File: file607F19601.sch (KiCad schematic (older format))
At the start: 14 parts, among them SW2 SW_SPDT, U2 MP2235

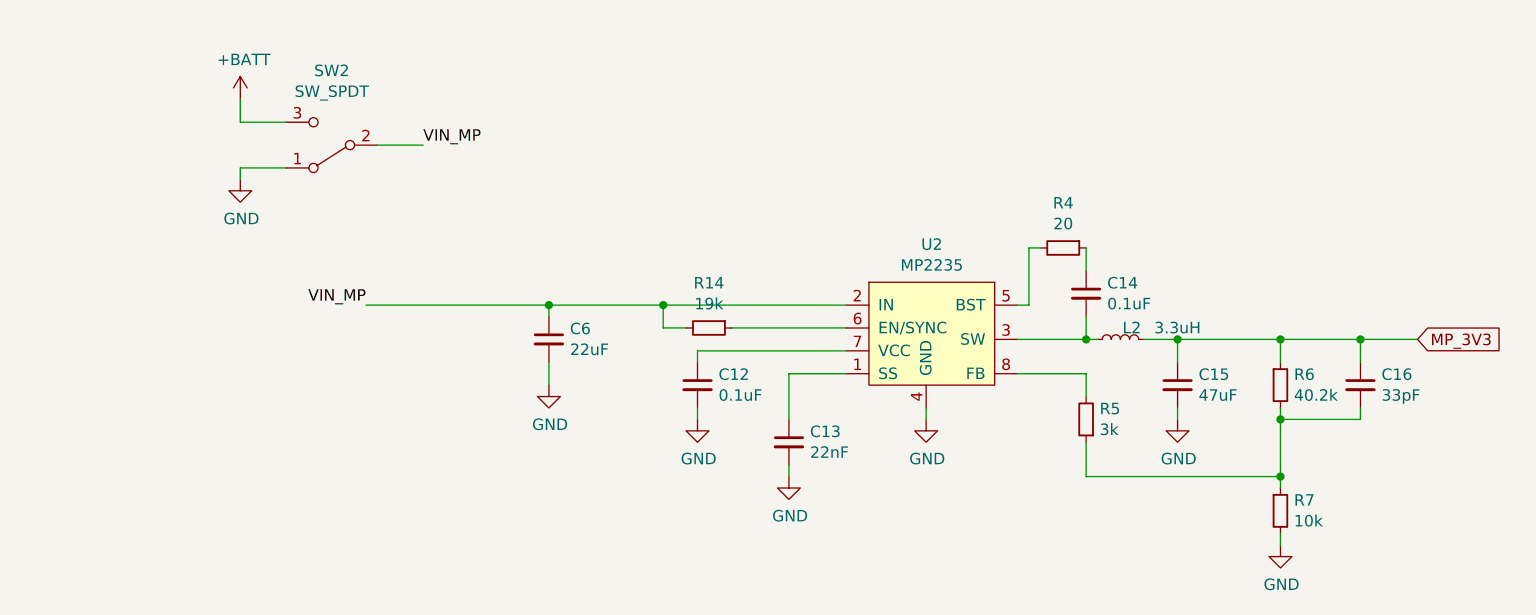
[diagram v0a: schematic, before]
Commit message: added data logging
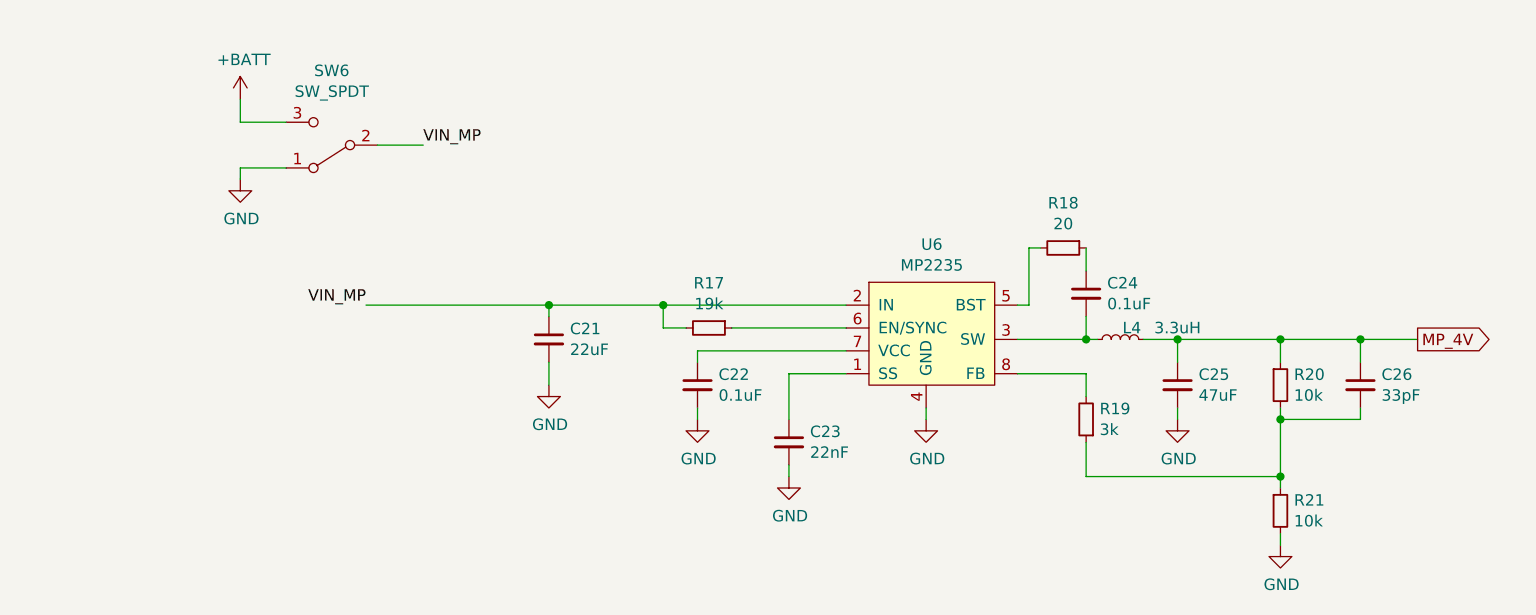
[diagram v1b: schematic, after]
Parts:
- R6: value 40.2k -> 10k
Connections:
- net MP_3V3 renamed MP_4V
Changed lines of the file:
@@
 $Descr A4 11693 8268
 encoding utf-8
-Sheet 4 10
+Sheet 9 10
 Title ""
 Date ""
@@
 AR Path="/607D64D2/607F1961/607F2E5A" Ref="C6"  Part="1"
 AR Path="/608CA2DC/608CBCF1/607F2E5A" Ref="C21"  Part="1"
-F 0 "C6" H 3342 3246 50  0000 L CNN
+F 0 "C21" H 3342 3246 50  0000 L CNN
 F 1 "22uF" H 3342 3155 50  0000 L CNN
 F 2 "" H 3250 3200 50  0001 C CNN
@@
 AR Path="/607D64D2/607F1961/607F34C1" Ref="#PWR05"  Part="1"
 AR Path="/608CA2DC/608CBCF1/607F34C1" Ref="#PWR0103"  Part="1"
-F 0 "#PWR05" H 3250 3150 50  0001 C CNN
+F 0 "#PWR0103" H 3250 3150 50  0001 C CNN
 F 1 "GND" H 3255 3227 50  0000 C CNN
 F 2 "" H 3250 3400 50  0001 C CNN
@@
 AR Path="/607D64D2/607F1961/60826F0B" Ref="C12"  Part="1"
 AR Path="/608CA2DC/608CBCF1/60826F0B" Ref="C22"  Part="1"
-F 0 "C12" H 3992 3446 50  0000 L CNN
+F 0 "C22" H 3992 3446 50  0000 L CNN
 F 1 "0.1uF" H 3992 3355 50  0000 L CNN
 F 2 "" H 3900 3400 50  0001 C CNN
@@
 AR Path="/607D64D2/607F1961/6082768B" Ref="#PWR012"  Part="1"
 AR Path="/608CA2DC/608CBCF1/6082768B" Ref="#PWR0104"  Part="1"
-F 0 "#PWR012" H 3900 3300 50  0001 C CNN
+F 0 "#PWR0104" H 3900 3300 50  0001 C CNN
 F 1 "GND" H 3905 3377 50  0000 C CNN
 F 2 "" H 3900 3550 50  0001 C CNN
@@
 AR Path="/607D64D2/607F1961/60827BCC" Ref="C13"  Part="1"
 AR Path="/608CA2DC/608CBCF1/60827BCC" Ref="C23"  Part="1"
-F 0 "C13" H 4392 3696 50  0000 L CNN
+F 0 "C23" H 4392 3696 50  0000 L CNN
 F 1 "22nF" H 4392 3605 50  0000 L CNN
 F 2 "" H 4300 3650 50  0001 C CNN
@@
 AR Path="/607D64D2/607F1961/60828452" Ref="#PWR013"  Part="1"
 AR Path="/608CA2DC/608CBCF1/60828452" Ref="#PWR0105"  Part="1"
-F 0 "#PWR013" H 4300 3550 50  0001 C CNN
+F 0 "#PWR0105" H 4300 3550 50  0001 C CNN
 F 1 "GND" H 4305 3627 50  0000 C CNN
 F 2 "" H 4300 3800 50  0001 C CNN
@@
 AR Path="/607D64D2/607F1961/608289FC" Ref="#PWR014"  Part="1"
 AR Path="/608CA2DC/608CBCF1/608289FC" Ref="#PWR0106"  Part="1"
-F 0 "#PWR014" H 4900 3300 50  0001 C CNN
+F 0 "#PWR0106" H 4900 3300 50  0001 C CNN
 F 1 "GND" H 4905 3377 50  0000 C CNN
 F 2 "" H 4900 3550 50  0001 C CNN
@@
 AR Path="/607D64D2/607F1961/60828F3D" Ref="#PWR015"  Part="1"
 AR Path="/608CA2DC/608CBCF1/60828F3D" Ref="#PWR0107"  Part="1"
-F 0 "#PWR015" H 6000 3300 50  0001 C CNN
+F 0 "#PWR0107" H 6000 3300 50  0001 C CNN
 F 1 "GND" H 6005 3377 50  0000 C CNN
 F 2 "" H 6000 3550 50  0001 C CNN
@@
 AR Path="/607D64D2/607F1961/608290F4" Ref="L2"  Part="1"
 AR Path="/608CA2DC/608CBCF1/608290F4" Ref="L4"  Part="1"
-F 0 "L2" V 5800 3150 50  0000 C CNN
+F 0 "L4" V 5800 3150 50  0000 C CNN
 F 1 "3.3uH" V 5800 2950 50  0000 C CNN
 F 2 "" H 5750 3200 50  0001 C CNN
@@
 AR Path="/607D64D2/607F1961/607F1BDD" Ref="U2"  Part="1"
 AR Path="/608CA2DC/608CBCF1/607F1BDD" Ref="U6"  Part="1"
-F 0 "U2" H 4925 3115 50  0000 C CNN
+F 0 "U6" H 4925 3115 50  0000 C CNN
 F 1 "MP2235" H 4925 3024 50  0000 C CNN
 F 2 "" H 4900 2950 50  0001 C CNN
@@
 AR Path="/607D64D2/607F1961/6082BD8B" Ref="C14"  Part="1"
 AR Path="/608CA2DC/608CBCF1/6082BD8B" Ref="C24"  Part="1"
-F 0 "C14" H 5692 3046 50  0000 L CNN
+F 0 "C24" H 5692 3046 50  0000 L CNN
 F 1 "0.1uF" H 5692 2955 50  0000 L CNN
 F 2 "" H 5600 3000 50  0001 C CNN
@@
 AR Path="/607D64D2/607F1961/6082C792" Ref="R4"  Part="1"
 AR Path="/608CA2DC/608CBCF1/6082C792" Ref="R18"  Part="1"
-F 0 "R4" V 5304 2800 50  0000 C CNN
+F 0 "R18" V 5304 2800 50  0000 C CNN
 F 1 "20" V 5395 2800 50  0000 C CNN
 F 2 "" H 5500 2800 50  0001 C CNN
@@
 AR Path="/607D64D2/607F1961/6082DC02" Ref="C15"  Part="1"
 AR Path="/608CA2DC/608CBCF1/6082DC02" Ref="C25"  Part="1"
-F 0 "C15" H 6092 3446 50  0000 L CNN
+F 0 "C25" H 6092 3446 50  0000 L CNN
 F 1 "47uF" H 6092 3355 50  0000 L CNN
 F 2 "" H 6000 3400 50  0001 C CNN
@@
 AR Path="/607D64D2/607F1961/6082EBBF" Ref="R6"  Part="1"
 AR Path="/608CA2DC/608CBCF1/6082EBBF" Ref="R20"  Part="1"
-F 0 "R6" H 6509 3446 50  0000 L CNN
-F 1 "40.2k" H 6509 3355 50  0000 L CNN
+F 0 "R20" H 6509 3446 50  0000 L CNN
+F 1 "10k" H 6509 3355 50  0000 L CNN
 F 2 "" H 6450 3400 50  0001 C CNN
 F 3 "~" H 6450 3400 50  0001 C CNN
@@
 AR Path="/607D64D2/607F1961/60830332" Ref="R7"  Part="1"
 AR Path="/608CA2DC/608CBCF1/60830332" Ref="R21"  Part="1"
-F 0 "R7" H 6509 3996 50  0000 L CNN
+F 0 "R21" H 6509 3996 50  0000 L CNN
 F 1 "10k" H 6509 3905 50  0000 L CNN
 F 2 "" H 6450 3950 50  0001 C CNN
@@
 AR Path="/607D64D2/607F1961/60830D4E" Ref="#PWR016"  Part="1"
 AR Path="/608CA2DC/608CBCF1/60830D4E" Ref="#PWR0108"  Part="1"
-F 0 "#PWR016" H 6450 3850 50  0001 C CNN
+F 0 "#PWR0108" H 6450 3850 50  0001 C CNN
 F 1 "GND" H 6455 3927 50  0000 C CNN
 F 2 "" H 6450 4100 50  0001 C CNN
@@
 AR Path="/607D64D2/607F1961/60831785" Ref="R5"  Part="1"
 AR Path="/608CA2DC/608CBCF1/60831785" Ref="R19"  Part="1"
-F 0 "R5" H 5541 3504 50  0000 R CNN
+F 0 "R19" H 5541 3504 50  0000 R CNN
 F 1 "3k" H 5541 3595 50  0000 R CNN
 F 2 "" H 5600 3550 50  0001 C CNN
@@
 AR Path="/607D64D2/607F1961/60836628" Ref="C16"  Part="1"
 AR Path="/608CA2DC/608CBCF1/60836628" Ref="C26"  Part="1"
-F 0 "C16" H 6892 3446 50  0000 L CNN
+F 0 "C26" H 6892 3446 50  0000 L CNN
 F 1 "33pF" H 6892 3355 50  0000 L CNN
 F 2 "" H 6800 3400 50  0001 C CNN
@@
 AR Path="/607D64D2/607F1961/6083C5A6" Ref="#PWR010"  Part="1"
 AR Path="/608CA2DC/608CBCF1/6083C5A6" Ref="#PWR0109"  Part="1"
-F 0 "#PWR010" H 1900 2000 50  0001 C CNN
+F 0 "#PWR0109" H 1900 2000 50  0001 C CNN
 F 1 "+BATT" H 1915 2323 50  0000 C CNN
 F 2 "" H 1900 2150 50  0001 C CNN
@@
 AR Path="/607D64D2/607F1961/6085AF61" Ref="SW2"  Part="1"
 AR Path="/608CA2DC/608CBCF1/6085AF61" Ref="SW6"  Part="1"
-F 0 "SW2" H 2300 2025 50  0000 C CNN
+F 0 "SW6" H 2300 2025 50  0000 C CNN
 F 1 "SW_SPDT" H 2300 2116 50  0000 C CNN
 F 2 "" H 2300 2350 50  0001 C CNN
@@
 AR Path="/607D64D2/607F1961/6085D770" Ref="#PWR011"  Part="1"
 AR Path="/608CA2DC/608CBCF1/6085D770" Ref="#PWR0110"  Part="1"
-F 0 "#PWR011" H 1900 2250 50  0001 C CNN
+F 0 "#PWR0110" H 1900 2250 50  0001 C CNN
 F 1 "GND" H 1905 2327 50  0000 C CNN
 F 2 "" H 1900 2500 50  0001 C CNN
@@
 AR Path="/607D64D2/607F1961/6080A4BD" Ref="R14"  Part="1"
 AR Path="/608CA2DC/608CBCF1/6080A4BD" Ref="R17"  Part="1"
-F 0 "R14" V 3754 3150 50  0000 C CNN
+F 0 "R17" V 3754 3150 50  0000 C CNN
 F 1 "19k" V 3845 3150 50  0000 C CNN
 F 2 "" H 3950 3150 50  0001 C CNN
@@
 Text Label 2700 2350 0    50   ~ 0
 VIN_MP
-Text GLabel 7050 3200 2    50   Input ~ 0
-MP_3V3
+Text GLabel 7050 3200 2    50   Output ~ 0
+MP_4V
 $EndSCHEMATC

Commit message: full schematic, version 1.0
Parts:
- removed SW2: SW_SPDT, symbol Switch:SW_SPDT
- added S6: EG1218, EIPP:EG1218, symbol EIPP_LIBRARY:EG1218
- C12, C13, C14, C16: footprint (none) -> Capacitor_SMD:C_0603_1608Metric_Pad1.08x0.95mm_HandSolder
- C15: footprint (none) -> Capacitor_SMD:C_1206_3216Metric_Pad1.33x1.80mm_HandSolder
- C6: footprint (none) -> Capacitor_SMD:C_0805_2012Metric_Pad1.18x1.45mm_HandSolder
- L2: footprint (none) -> EIPP:HM66M
- R14, R5, R6, R7: footprint (none) -> Resistor_SMD:R_0805_2012Metric_Pad1.20x1.40mm_HandSolder
- R4: footprint (none) -> Resistor_SMD:R_0603_1608Metric_Pad0.98x0.95mm_HandSolder
- U2: footprint (none) -> EIPP:SOT65P280X100-8N
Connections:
- net +BATT: now also S6.S
- net GND: now also S6.O
- net VIN_MP: now also S6.P

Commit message: component layout complete
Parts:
- R6: value 10k -> 40.2k
- R7: value 10k -> 10.2k
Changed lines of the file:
@@
 Wire Wire Line
 	6000 3200 6000 3300
-$Comp
-L Device:C_Small C15
-U 1 1 6082DC02
-P 6000 3400
-AR Path="/607D64D2/607F1961/6082DC02" Ref="C15"  Part="1"
-AR Path="/608CA2DC/608CBCF1/6082DC02" Ref="C25"  Part="1"
-F 0 "C25" H 6092 3446 50  0000 L CNN
-F 1 "47uF" H 6092 3355 50  0000 L CNN
-F 2 "Capacitor_SMD:C_1206_3216Metric_Pad1.33x1.80mm_HandSolder" H 6000 3400 50  0001 C CNN
-F 3 "~" H 6000 3400 50  0001 C CNN
-	1    6000 3400
-	1    0    0    -1
-$EndComp
 Wire Wire Line
 	6000 3200 6450 3200
@@
 AR Path="/608CA2DC/608CBCF1/608F2861" Ref="R20"  Part="1"
 F 0 "R20" H 6509 3446 50  0000 L CNN
-F 1 "10k" H 6509 3355 50  0000 L CNN
+F 1 "40.2k" H 6509 3355 50  0000 L CNN
 F 2 "Resistor_SMD:R_0805_2012Metric_Pad1.20x1.40mm_HandSolder" H 6450 3400 50  0001 C CNN
 F 3 "~" H 6450 3400 50  0001 C CNN
@@
 AR Path="/608CA2DC/608CBCF1/608F2862" Ref="R21"  Part="1"
 F 0 "R21" H 6509 3996 50  0000 L CNN
-F 1 "10k" H 6509 3905 50  0000 L CNN
+F 1 "10.2k" H 6509 3905 50  0000 L CNN
 F 2 "Resistor_SMD:R_0805_2012Metric_Pad1.20x1.40mm_HandSolder" H 6450 3950 50  0001 C CNN
 F 3 "~" H 6450 3950 50  0001 C CNN
@@
 Wire Wire Line
 	1650 2300 2050 2300
+$Comp
+L Device:C_Small C15
+U 1 1 6082DC02
+P 6000 3400
+AR Path="/607D64D2/607F1961/6082DC02" Ref="C15"  Part="1"
+AR Path="/608CA2DC/608CBCF1/6082DC02" Ref="C25"  Part="1"
+F 0 "C25" H 6092 3446 50  0000 L CNN
+F 1 "47uF" H 6092 3355 50  0000 L CNN
+F 2 "Capacitor_SMD:C_1206_3216Metric_Pad1.33x1.80mm_HandSolder" H 6000 3400 50  0001 C CNN
+F 3 "~" H 6000 3400 50  0001 C CNN
+	1    6000 3400
+	1    0    0    -1
+$EndComp
 $EndSCHEMATC
